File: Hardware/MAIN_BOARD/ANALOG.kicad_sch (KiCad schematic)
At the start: 547 parts, among them J1 NC3MBH-B, J13 Conn_02x08_Odd_Even, J2 NC3MBH-B, J9 Conn_01x03_Pin, K1 EC2-5NU, K2 EC2-5NU, Q5 BC847, U10 SN74LVC245AN, U11 SN74LVC1G04DBVR, U16 SI8660BC-B-IS1R, U17 SI8660BC-B-IS1R, U18 SI8660BC-B-IS1R, U2 74LS595, U29 SN74LVC245AN, U3 SN74LVC245AN, U30 74LS595, U31 SN74LVC245AN, U32 SN74LVC245AN, U33 74LS595, U34 SN74LVC245AN, U35 SN74LVC245AN, U36 74LS595, U37 SN74LVC245AN, U38 SN74LVC1G04DBVR, U39 SN74LVC1G04DBVR, U4 SN74LVC245AN, U40 SN74LVC1G04DBVR, U41 SN74LVC245AN, U42 SN74LVC245AN, U43 74LS595, U44 74LS595, U45 SN74LVC245AN, U46 SN74LVC245AN, U47 SN74LVC245AN, U48 SN74LVC245AN, U49 74LS595, U5 SN74LVC245AN, U50 74LS595, U51 SN74LVC245AN, U52 SN74LVC245AN, U53 SN74LVC245AN, U54 SN74LVC245AN, U55 74LS595, U56 74LS595, U57 SN74LVC245AN, U58 SN74LVC245AN, U59 SN74LVC1G04DBVR, U6 74LS595, U60 SN74LVC1G04DBVR, U62 SN74LVC1G04DBVR, U64 OPA2134UA, U66 OPA2134UA, U7 SN74LVC245AN, U8 SN74LVC245AN, U9 74LS595

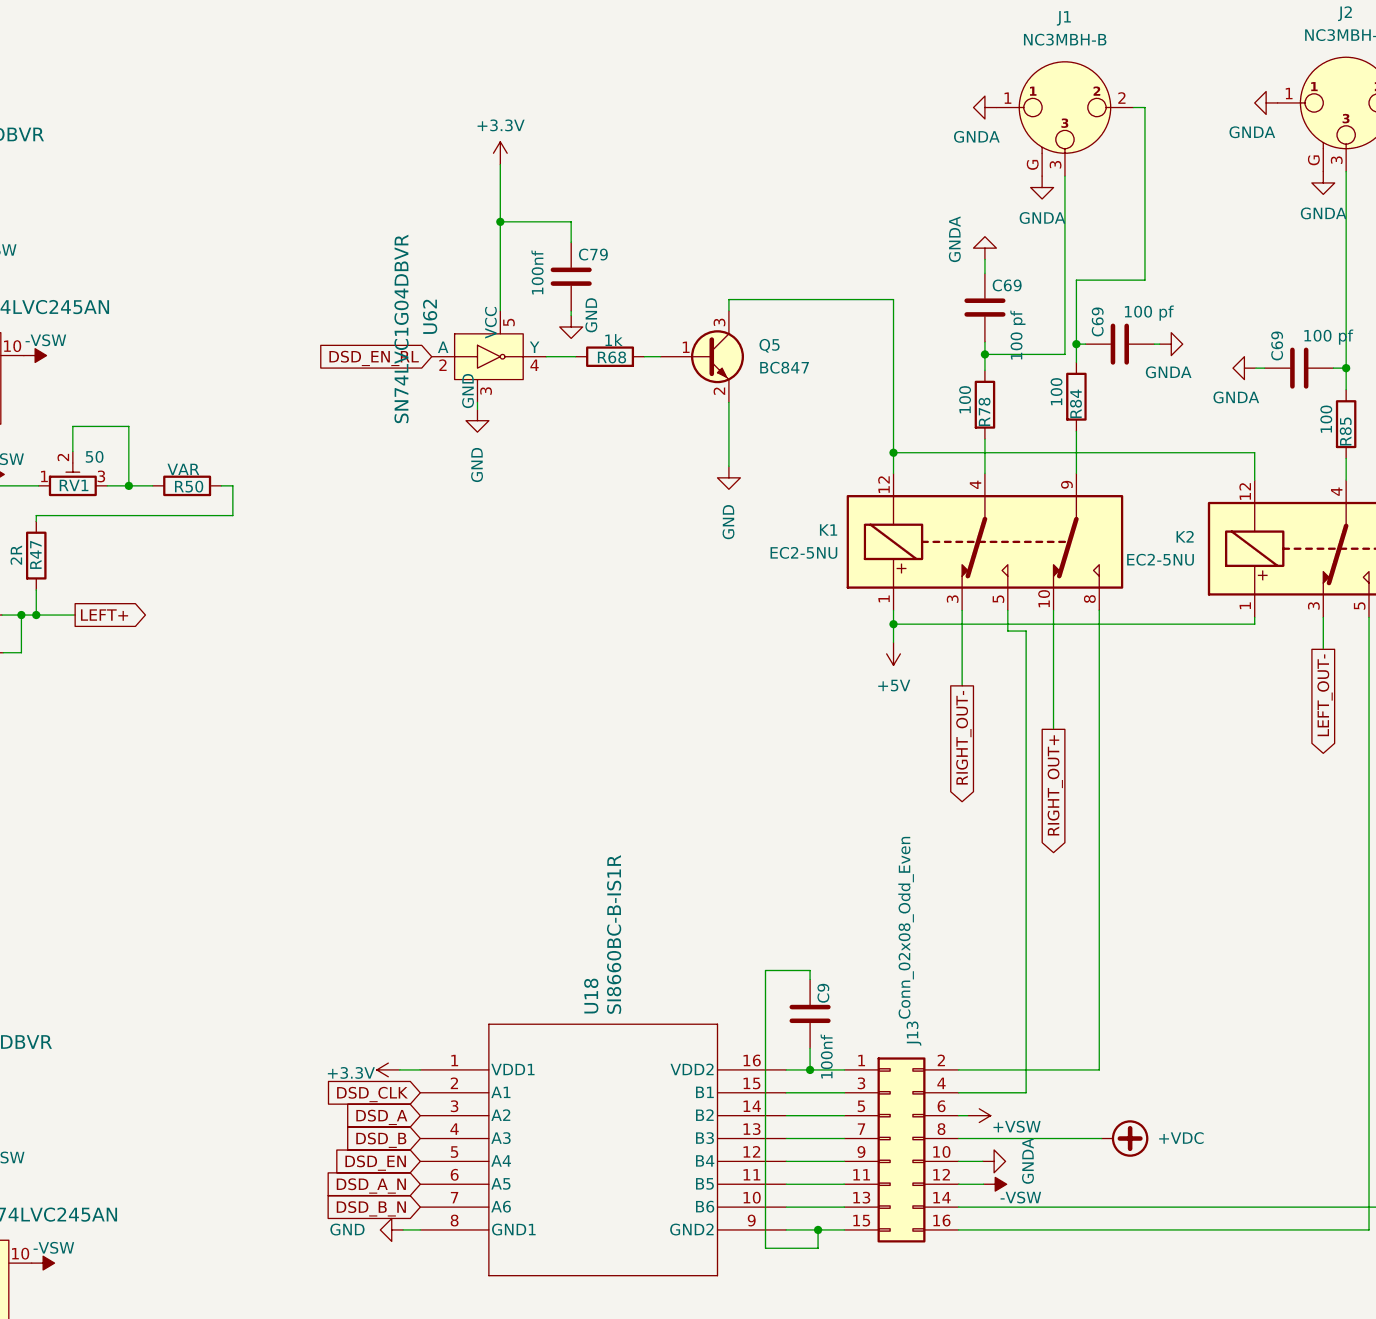
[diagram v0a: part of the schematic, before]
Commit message: some PCB/schemtic improvements
some PCB improvements,
three additional debug LEDs,
add serial res. at data/clk line
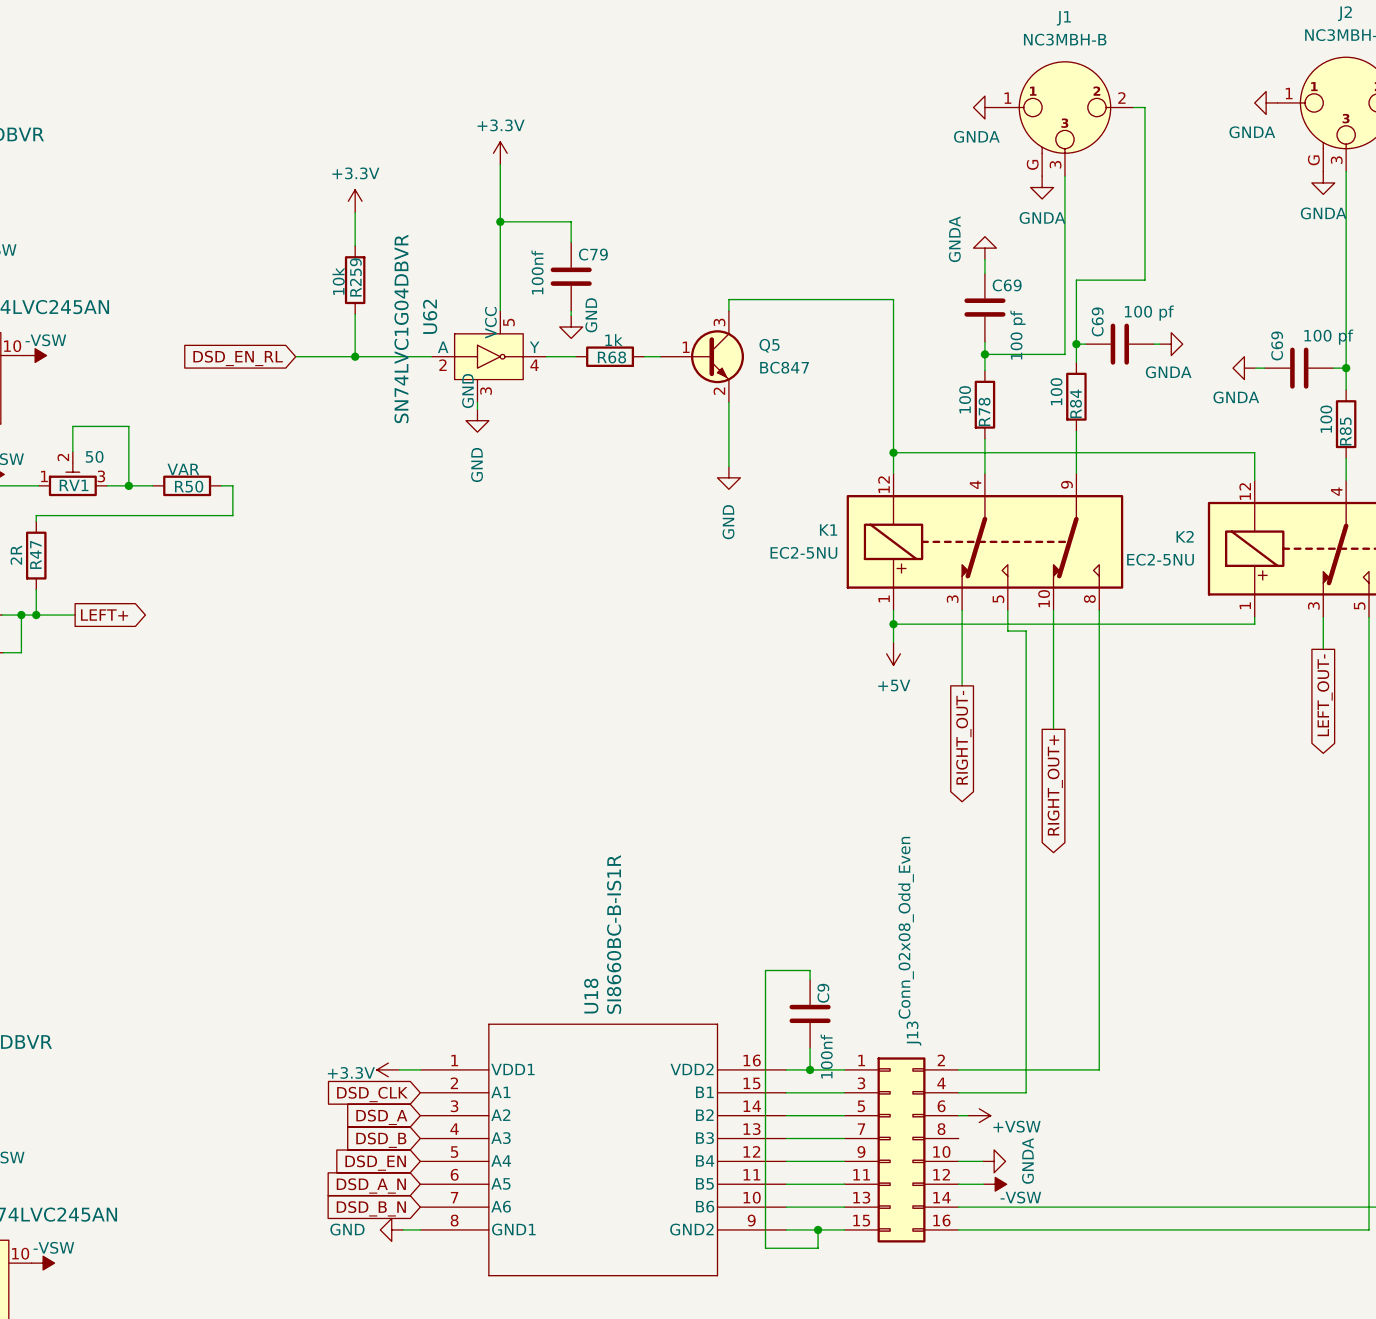
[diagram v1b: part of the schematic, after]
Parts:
- added R259: 10k, PCM_Resistor_SMD_AKL:R_0603_1608Metric, symbol PCM_Resistor_AKL:R_0402
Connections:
- net +3.3V: now also R259.2
- net DSD_EN_RL: now also R259.1
- net +VDC: no longer names the net of J13.8 (Pin_8)
